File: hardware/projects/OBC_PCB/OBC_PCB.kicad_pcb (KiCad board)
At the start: 8 copper layers, 42.2 x 67.2 mm, 171 parts, among them J1 LS021B7DD02, J2 DM3CS-SF, J3 FH12-12S-0.5SH(55), J4 1S Li-Po, J5 TC2030-CTX-NL, J7 RF coax pads, J8 RF coax pads, Q1 AO3400A, SW1 PREV, SW2 NEXT, SW3 SELECT / POWER, SW4 BACK, U1 MAX-F11N, U10 SN74LVC2G00DCTR, U2 nPM1300-QEAA, U3 BMA400, U4 LIS2MDL, U5 BMP581, U6 nRF54LM20A-QGAA, U7 TPS63900DSKR, U8 SN74LVC02APWR, U9 LP5810BDSDR, Y1 32MHz, Y3 32.768kHz

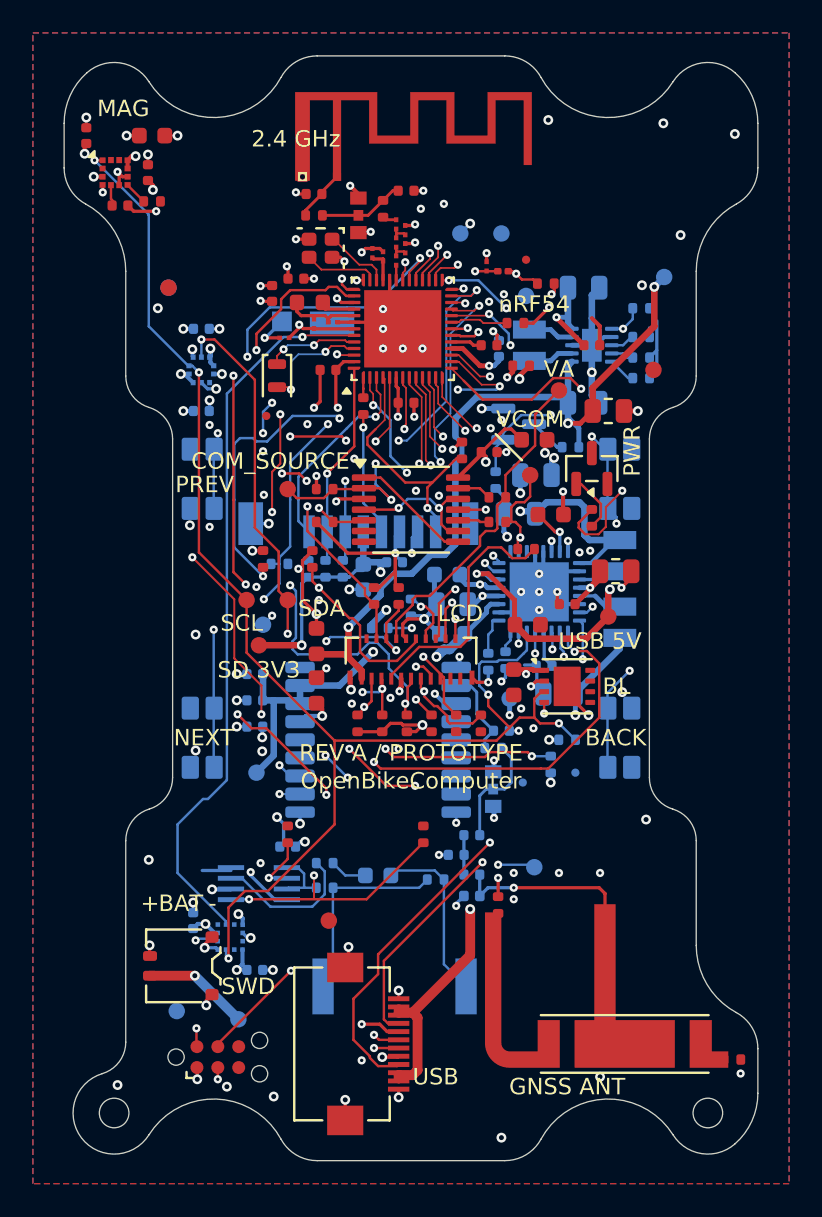
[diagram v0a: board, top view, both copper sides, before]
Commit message: hardware: finalize shielded board placement and display flex integration
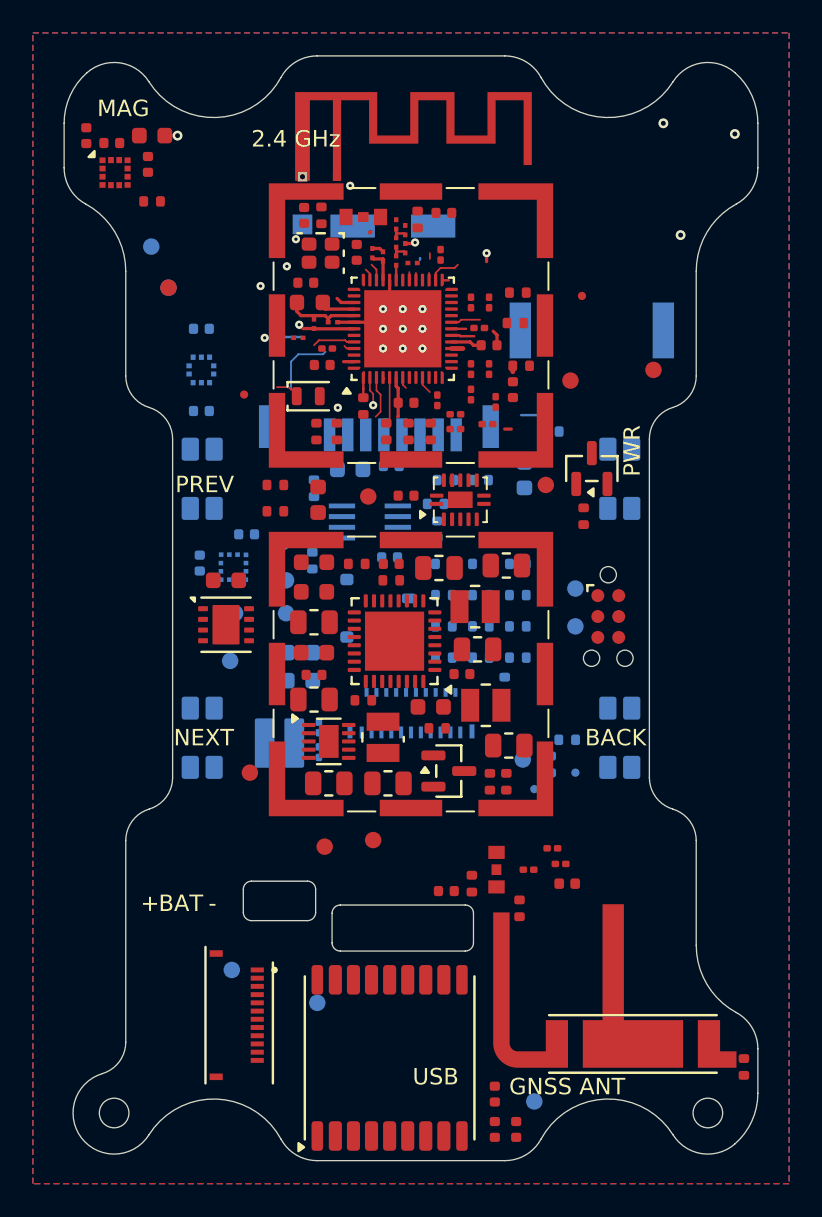
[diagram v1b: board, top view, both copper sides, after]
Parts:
- added J6: BACKLIGHT A/K - PROVISIONAL SOLDER, obc:Backlight_Flex_Solder_2_P1.8mm_Provisional, B.Cu at (92.0, 108.2)
- added R69: 100, Resistor_SMD:R_0201_0603Metric, F.Cu at (102.7, 88.2)
- added R70: 100, Resistor_SMD:R_0201_0603Metric, F.Cu at (101.6, 87.3)
- added R71: 100, Resistor_SMD:R_0201_0603Metric, F.Cu at (104.8, 85.5)
- added R72: 100, Resistor_SMD:R_0201_0603Metric, F.Cu at (104.8, 81.4)
- added R73: 100, Resistor_SMD:R_0201_0603Metric, F.Cu at (104.2, 83.0)
- added R74: 100, Resistor_SMD:R_0201_0603Metric, F.Cu at (103.7, 81.4)
- added R75: 100, Resistor_SMD:R_0201_0603Metric, F.Cu at (103.7, 85.5)
- added R76: 220, Resistor_SMD:R_0201_0603Metric, F.Cu at (105.2, 87.5)
- added R77: 220, Resistor_SMD:R_0201_0603Metric, F.Cu at (102.7, 89.1)
- added R78: 220, Resistor_SMD:R_0201_0603Metric, F.Cu at (103.7, 87.0)
- added R79: 220, Resistor_SMD:R_0201_0603Metric, F.Cu at (94.9, 84.2)
- added R80: 220, Resistor_SMD:R_0201_0603Metric, F.Cu at (104.7, 88.8)
- added SH1: BMI-S-202-F-20-R, obc:Laird_BMI-S-202-F-20_16.5mm, F.Cu at (100.0, 82.8)
- added SH2: BMI-S-202-F-20-R, obc:Laird_BMI-S-202-F-20_16.5mm, F.Cu at (100.0, 104.0)
- C1, C10, C14, C15, C2, C26, C28, C29, C30, C4, C5, C50, C7, C8, J8, L1, L2, L5, L7, Q1, R1, R2, R28, R29, R3, R31, R32, R40, R63, R66, R67, TP10, TP7, U1, U2, U7: moved to F.Cu
- C27, C31, C32: footprint Capacitor_SMD:C_0402_1005Metric -> Capacitor_SMD:C_0201_0603Metric; moved to F.Cu
- C39, C40, J1, J4, R44, R45, R48, R49, R50, R51, R53, R54, R55, R57, R58, R59, R60, R61, R62, TP11, TP12, TP13, TP9: moved to B.Cu
- J3: value FH12-12S-0.5SH(55) -> FH34SRJ-12S-0.5SH(50); footprint Connector_FFC-FPC:Hirose_FH12-12S-0.5SH_1x12-1MP_P0.50mm_Horizontal -> obc:Hirose_FH34SRJ_12S_0.5SH
- R64, R65: footprint Resistor_SMD:R_0402_1005Metric -> Resistor_SMD:R_0201_0603Metric
- U8: value SN74LVC02APWR -> SN74LVC02ABQAR; footprint Package_SO:TSSOP-14_4.4x5mm_P0.65mm -> Package_DFN_QFN:DHWQFN-14-1EP_2.5x3mm_P0.5mm_EP1x1.5mm
- moved TP6 47.7 mm to (89.1, 122.0)
- moved BZ1 41.7 mm to (111.0, 83.1)
- moved TP10 38.6 mm to (97.7, 114.1)
- moved J5 35.8 mm to (112.0, 100.5), turned to -90 degrees
- moved C28 31.9 mm to (106.4, 131.7), turned to 90 degrees
- moved R65 30.0 mm to (94.4, 108.8), turned to 90 degrees
- moved C8 29.9 mm to (94.1, 105.5), turned to 180 degrees
- moved C29 29.9 mm to (105.1, 131.7), turned to 90 degrees
- moved R64 29.8 mm to (94.4, 107.2), turned to 90 degrees
- moved TP5 29.5 mm to (89.0, 103.2)
- moved U7 28.9 mm to (95.0, 108.1), turned to 0 degrees
- moved R3 28.4 mm to (101.6, 107.3)
- moved C9 28.3 mm to (95.0, 110.7), turned to 180 degrees
- moved R34 28.1 mm to (108.5, 89.2)
- moved R63 27.8 mm to (97.1, 105.6)
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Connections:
- J1 pad 1: +5V_DISP -> unconnected-(J1-NC-Pad1)
- J1 pad 10: GND -> /LCD_BCK
- J1 pad 12: /LCD_BCK -> GND
- J1 pad 13: /LCD_R0 -> +3V2
- J1 pad 14: /LCD_R1 -> Net-(J1-VA)
- J1 pad 15: /LCD_G0 -> Net-(J1-VB)
- J1 pad 16: /LCD_G1 -> /LCD_INTB
- J1 pad 17: /LCD_B0 -> /LCD_GEN
- J1 pad 18: /LCD_B1 -> /LCD_GCK
- J1 pad 19: unconnected-(J1-NC-Pad19) -> /LCD_GSP
- J1 pad 2: unconnected-(J1-NC-Pad2) -> Net-(J1-VCOM)
- J1 pad 20: Net-(J1-VCOM) -> unconnected-(J1-NC-Pad20)
- J1 pad 21: unconnected-(J1-NC-Pad21) -> +5V_DISP
- J1 pad 3: /LCD_GSP -> unconnected-(J1-NC-Pad3)
- J1 pad 4: /LCD_GCK -> /LCD_B1
- J1 pad 5: /LCD_GEN -> /LCD_B0
- J1 pad 6: /LCD_INTB -> /LCD_G1
- J1 pad 7: Net-(J1-VB) -> /LCD_G0
- J1 pad 8: Net-(J1-VA) -> /LCD_R1
- J1 pad 9: +3V2 -> /LCD_R0
- U6 pad 11: /LCD_GSP -> /LCD_GSP_MCU
- U6 pad 12: /LCD_GEN -> /LCD_GEN_MCU
- U6 pad 13: /SCL -> /LCD_BSP_MCU
- U6 pad 14: /SDA -> /LCD_GCK_MCU
- U6 pad 15: /LCD_BCK -> /LCD_BCK_MCU
- U6 pad 16: /LCD_G0 -> /LCD_G0_MCU
- U6 pad 22: /LCD_G1 -> /LCD_G1_MCU
- U6 pad 23: /LCD_B0 -> /LCD_B0_MCU
- U6 pad 24: /LCD_B1 -> /LCD_B1_MCU
- U6 pad 26: /BTN_PREV -> /BTN_SELECT
- U6 pad 39: /BTN_SELECT -> /BTN_PREV
- U6 pad 40: /LCD_GCK -> /SDA
- U6 pad 41: /LCD_BSP -> /SCL
- U6 pad 50: /LCD_INTB -> /LCD_INTB_MCU
- U6 pad 8: /LCD_R0 -> /LCD_R0_MCU
- U6 pad 9: /LCD_R1 -> /LCD_R1_MCU
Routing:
- net GND: track 136.5 -> 10.7 mm, vias 115 -> 20
- net /SDA: track 116.5 -> 0.00 mm, vias 10 -> 0
- net /SCL: track 113.3 -> 0.00 mm, vias 7 -> 0
- net /nRESET: track 69.7 -> 0.00 mm, vias 3 -> 0
- net /SWDIO: track 59.5 -> 0.59 mm, vias 3 -> 0
- net /LCD_B1: track 57.0 -> 0.00 mm, vias 6 -> 0
- net /BUZZER_PWM: track 82.3 -> 25.8 mm, vias 8 -> 0
- net /Power Management/SHPHLD: track 54.7 -> 0.00 mm, vias 6 -> 0
- net /LCD_G1: track 54.6 -> 0.00 mm, vias 6 -> 0
- net /COM_EN: track 52.1 -> 0.00 mm, vias 5 -> 0
- net /PMIC_INT: track 65.0 -> 14.1 mm, vias 5 -> 0
- net /SWDCLK: track 62.4 -> 11.8 mm, vias 4 -> 0
- net +3V2: track 54.1 -> 4.79 mm, vias 33 -> 1
- net +5V_DISP: track 48.3 -> 0.00 mm, vias 3 -> 0
- net VSYS: track 47.9 -> 0.00 mm, vias 5 -> 0
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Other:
- outline, holes or cut-outs redrawn
- board text added: "B.Cu ground + stitching between SD and GNSS; keep SD transitions north of the socket contact row"
- board text added: "BACKLIGHT: U9 driver and provisional J6 solder pads. Confirm LED stack, load and flex with supplier."
- board text added: "BL FLEX SLOT 4.4 x 2.4 R0.5"
- board text added: "GNSS: retain J8 coax pads, R40 isolation link and all tuning footprints. Corridor/antenna coupling needs assembled reception tests. Keep unrelated signals and vias out of the RF corridor."
- board text added: "J3 follows the USB flex model; keep the insertion lane clear. J4 underside: mate battery before seating the PCB/display unit. Allow a service loop; J6 and battery lead details remain provisional."
- board text added: "J5: TC2030-CTX-NL. Factory SWD access before display assembly. No paste. Keep 0.508mm from unrelated tracks; preserve probe access."
- board text added: "J6 PROVISIONAL SOLDER PADS: verify tail, A/K, LED load, solder process and strain relief with supplier before fabrication."
- board text added: "LCD FLEX SLOT 8.6 x 2.8 R0.5; center (99.50,119.45)"
- board text added: "PLACEMENT CHECKPOINT - ROUTING INCOMPLETE LCD-to-cover: 0.50mm. Rear optical material: 0.70mm + 0.10mm assembly gap. SH1 + SH2: BMI-S-202-F-20-R frames; fit BMI-S-202-C-20 lids. Keep enclosed parts below 1.8mm. Bond frames with a close GND via fence. J3: FH34SRJ-12S-0.5SH(50), gold tail 0.30 +/-0.03mm thick, 6.50 +/-0.05mm wide."
- board text added: "ROUTE FIRST: GNSS RF on F.Cu; drawing is a guide, not copper. Use continuous In1.Cu GND under the slot-side corridor. 0.18mm provisional width; confirm 50R with fabricator. Keep J8 accessible; tune and test L1/L5 in the complete enclosure."
- board text added: "ROUTE FIRST: USB 90R on In5.Cu Use west corridor around H3; keep reference planes continuous"
- board text removed: "3V2"
- board text removed: "5V"
- board text removed: "ACCEL"
- board text removed: "BACKLIGHT: U9 driver fitted. J6 connector and LED load remain undefined."
- board text removed: "BL"
- board text removed: "BOOT"
- board text removed: "COM_SOURCE"
- board text removed: "DISP 5V"
- board text removed: "GND"
- board text removed: "GNSS"
- board text removed: "GNSS REVIEW: BSP, GEN and SHPHLD retain short B.Cu paths under U1. Preserve L7 ground. Qualify GNSS with display refresh, buzzer PWM and power-state changes in the final enclosure."
- board text removed: "J5: TC2030-CTX-NL. No paste. Keep 0.508mm from other tracks; clear probe access."
- board text removed: "LCD"
- board text removed: "OpenBikeComputer"
- board text removed: "PMIC"
- board text removed: "REV A / PROTOTYPE"
- board text removed: "RF"
- board text removed: "SCL"
- board text removed: "SD 3V3"
- board text removed: "SDA"
- board text removed: "SHPHLD"
- board text removed: "SWD"
- board text removed: "USB 5V"
- board text removed: "USB and battery connector positions remain provisional. Backlight connector pending."
- board text removed: "VA"
- board text removed: "VCOM"
- board text removed: "VSYS"
- board text removed: "nRF54"
